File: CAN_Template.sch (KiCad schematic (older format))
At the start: 18 parts, among them U5 MCP2515-xSO, U6 SN65HVD1050D

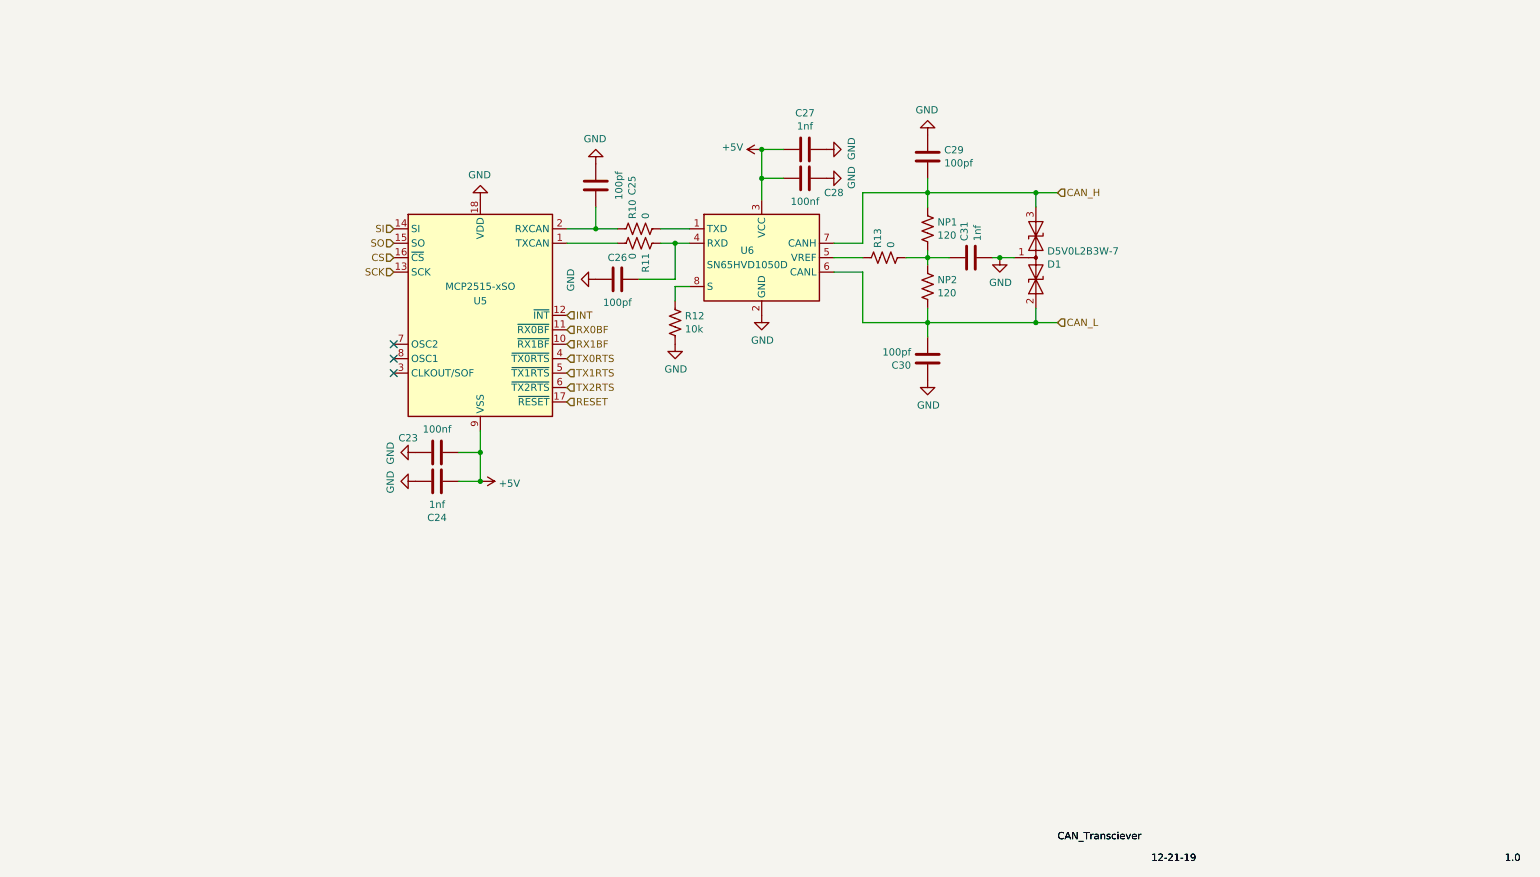
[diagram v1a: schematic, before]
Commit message: Changed filter and fixed CAN circuit
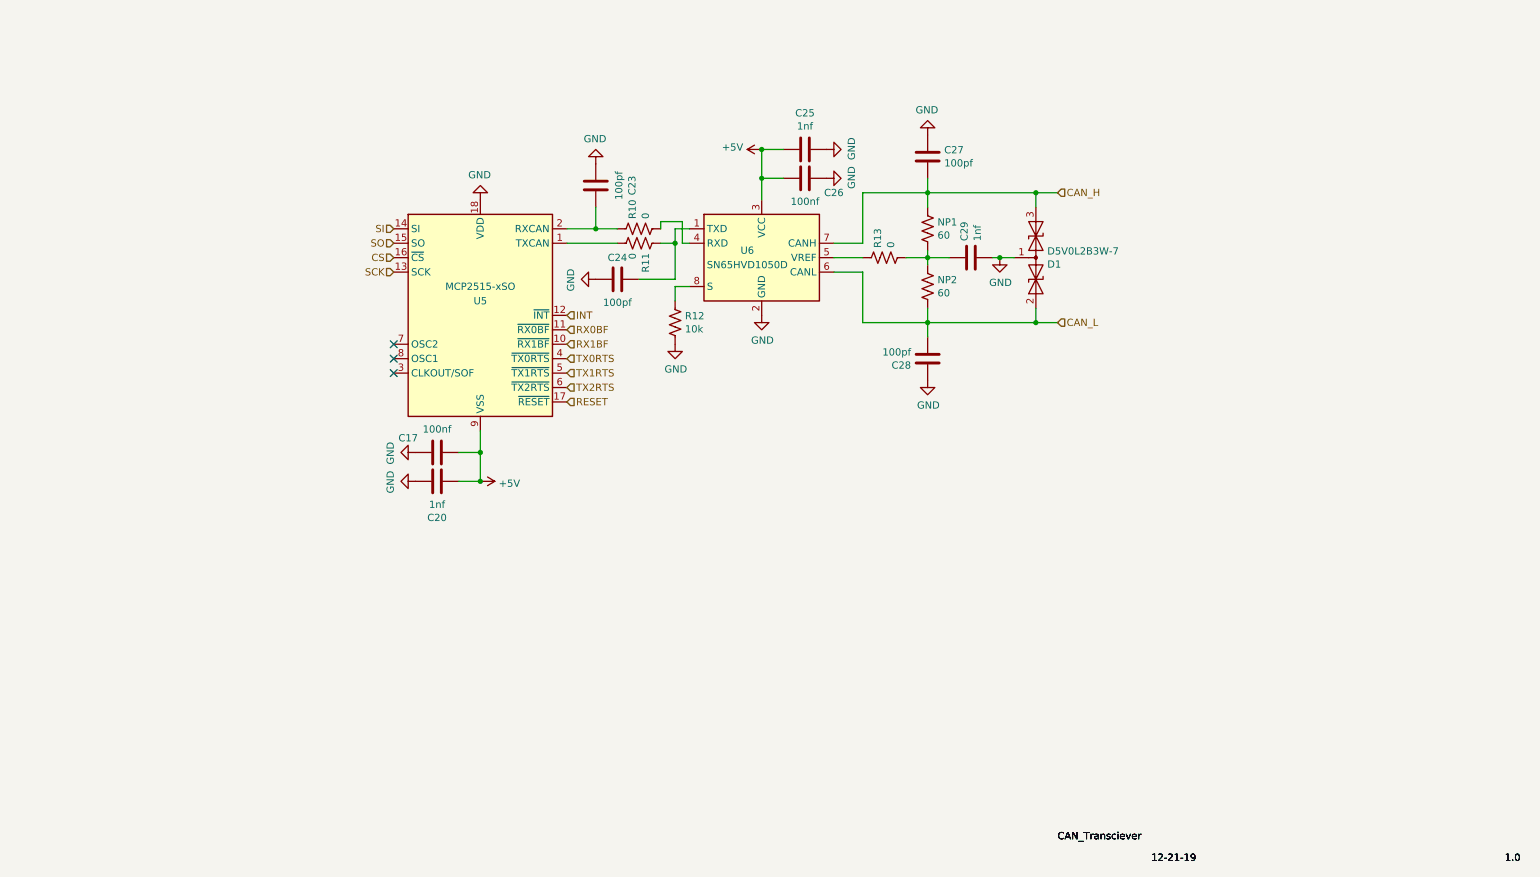
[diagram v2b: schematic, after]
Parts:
- NP1, NP2: value 120 -> 60
- renumbered C23 to C17, C24 to C20, C25 to C23, C26 to C24, C27 to C25, C28 to C26, C29 to C27, C30 to C28, C31 to C29
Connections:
- net at U6.1 (TXD): now also C24.2, R11.1; no longer R10.2
- new net: R10.2, U6.4 (RXD)
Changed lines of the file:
@@
 EESchema Schematic File Version 4
 LIBS:BLEANT-cache
+LIBS:CAN_Template-cache
 EELAYER 30 0
 EELAYER END
@@
 Text Label 7500 7500 0    50   ~ 0
 CAN_Transciever
+Text Label 10600 7650 0    50   ~ 0
+1.0
+Text Label 8150 7650 0    50   ~ 0
+12-21-19
+Text Label 7500 7500 0    50   ~ 0
+CAN_Transciever
 $Comp
 L Device:R_US NP1
@@
 P 6600 3250
 F 0 "NP1" H 6668 3296 50  0000 L CNN
-F 1 "120" H 6668 3205 50  0000 L CNN
+F 1 "60" H 6668 3205 50  0000 L CNN
 F 2 "Resistor_SMD:R_0402_1005Metric" V 6640 3240 50  0001 C CNN
 F 3 "~" H 6600 3250 50  0001 C CNN
@@
 $EndComp
 $Comp
-L Device:C C25
+L Device:C C23
 U 1 1 5DCB7D7B
 P 4300 2950
-F 0 "C25" V 4048 2950 50  0000 C CNN
+F 0 "C23" V 4048 2950 50  0000 C CNN
 F 1 "100pf" V 4139 2950 50  0000 C CNN
 F 2 "Capacitor_SMD:C_0402_1005Metric" H 4338 2800 50  0001 C CNN
@@
 $EndComp
 $Comp
-L Device:C C27
+L Device:C C25
 U 1 1 5DCB9CD1
 P 5750 2700
-F 0 "C27" V 5498 2700 50  0000 C CNN
+F 0 "C25" V 5498 2700 50  0000 C CNN
 F 1 "1nf" V 5589 2700 50  0000 C CNN
 F 2 "Capacitor_SMD:C_0402_1005Metric" H 5788 2550 50  0001 C CNN
@@
 $EndComp
 $Comp
-L Device:C C28
+L Device:C C26
 U 1 1 5DCBAD85
 P 5750 2900
-F 0 "C28" V 5650 2700 50  0000 C CNN
+F 0 "C26" V 5650 2700 50  0000 C CNN
 F 1 "100nf" V 5589 2900 50  0000 C CNN
 F 2 "Capacitor_SMD:C_0402_1005Metric" H 5788 2750 50  0001 C CNN
@@
 $EndComp
 $Comp
-L Device:C C30
+L Device:C C28
 U 1 1 5DCE6703
 P 6600 4150
-F 0 "C30" H 6715 4196 50  0000 L CNN
+F 0 "C28" H 6715 4196 50  0000 L CNN
 F 1 "100pf" H 6715 4105 50  0000 L CNN
 F 2 "Capacitor_SMD:C_0402_1005Metric" H 6638 4000 50  0001 C CNN
@@
 P 6600 3650
 F 0 "NP2" H 6668 3696 50  0000 L CNN
-F 1 "120" H 6668 3605 50  0000 L CNN
+F 1 "60" H 6668 3605 50  0000 L CNN
 F 2 "Resistor_SMD:R_0402_1005Metric" V 6640 3640 50  0001 C CNN
 F 3 "~" H 6600 3650 50  0001 C CNN
@@
 $EndComp
 $Comp
-L Device:C C31
+L Device:C C29
 U 1 1 5DCEFDFD
 P 6900 3450
-F 0 "C31" H 7015 3496 50  0000 L CNN
+F 0 "C29" H 7015 3496 50  0000 L CNN
 F 1 "1nf" H 7015 3405 50  0000 L CNN
 F 2 "Capacitor_SMD:C_0402_1005Metric" H 6938 3300 50  0001 C CNN
@@
 $EndComp
 $Comp
+L Device:D_TVS_x2_CAA D1
+U 1 1 5DD0169A
+P 7350 3450
+F 0 "D1" V 7304 3529 50  0000 L CNN
+F 1 "D5V0L2B3W-7" V 7395 3529 50  0000 L CNN
+F 2 "Package_TO_SOT_SMD:SOT-23" H 7200 3450 50  0001 C CNN
+F 3 "https://www.mouser.com/datasheet/2/115/D5V0L2B3W-218988.pdf" H 7200 3450 50  0001 C CNN
+	1    7350 3450
+	0    1    -1   0
+$EndComp
+$Comp
 L Device:R_US R12
 U 1 1 5DD5BD7B
@@
 CAN_H
 $Comp
-L Device:C C29
+L Device:C C27
 U 1 1 5DCE5998
 P 6600 2750
-F 0 "C29" H 6715 2796 50  0000 L CNN
+F 0 "C27" H 6715 2796 50  0000 L CNN
 F 1 "100pf" H 6715 2705 50  0000 L CNN
 F 2 "Capacitor_SMD:C_0402_1005Metric" H 6638 2600 50  0001 C CNN
@@
 $EndComp
 $Comp
-L Device:C C24
+L Device:C C20
 U 1 1 5E0BDAE5
 P 3200 5000
-F 0 "C24" V 2948 5000 50  0000 C CNN
+F 0 "C20" V 2948 5000 50  0000 C CNN
 F 1 "1nf" V 3039 5000 50  0000 C CNN
 F 2 "Capacitor_SMD:C_0402_1005Metric" H 3238 4850 50  0001 C CNN
@@
 $EndComp
 $Comp
-L Device:C C23
+L Device:C C17
 U 1 1 5E0BDAEB
 P 3200 4800
-F 0 "C23" V 3100 4600 50  0000 C CNN
+F 0 "C17" V 3100 4600 50  0000 C CNN
 F 1 "100nf" V 3039 4800 50  0000 C CNN
 F 2 "Capacitor_SMD:C_0402_1005Metric" H 3238 4650 50  0001 C CNN
@@
 Connection ~ 3500 5000
 $Comp
-L Device:C C26
+L Device:C C24
 U 1 1 5E0C191D
 P 4450 3600
-F 0 "C26" V 4600 3600 50  0000 C CNN
+F 0 "C24" V 4600 3600 50  0000 C CNN
 F 1 "100pf" V 4289 3600 50  0000 C CNN
 F 2 "Capacitor_SMD:C_0402_1005Metric" H 4488 3450 50  0001 C CNN
@@
 Wire Wire Line
 	4850 3600 4850 3350
-Connection ~ 4850 3350
-Wire Wire Line
-	4850 3350 4950 3350
 Wire Wire Line
 	4300 3100 4300 3250
@@
 Wire Wire Line
 	4300 3250 4450 3250
-Wire Wire Line
-	4750 3250 4950 3250
 NoConn ~ 2900 4050
 NoConn ~ 2900 4150
@@
 Text Label 7500 7500 0    50   ~ 0
 CAN_Transciever
-$Comp
-L Device:D_TVS_x2_CAA D1
-U 1 1 5DD0169A
-P 7350 3450
-F 0 "D1" V 7304 3529 50  0000 L CNN
-F 1 "D5V0L2B3W-7" V 7395 3529 50  0000 L CNN
-F 2 "Package_TO_SOT_SMD:SOT-23" H 7200 3450 50  0001 C CNN
-F 3 "https://www.mouser.com/datasheet/2/115/D5V0L2B3W-218988.pdf" H 7200 3450 50  0001 C CNN
-	1    7350 3450
-	0    1    -1   0
-$EndComp
+Wire Wire Line
+	4850 3350 4850 3250
+Wire Wire Line
+	4850 3250 4950 3250
+Connection ~ 4850 3350
+Wire Wire Line
+	4750 3250 4750 3200
+Wire Wire Line
+	4750 3200 4900 3200
+Wire Wire Line
+	4900 3200 4900 3350
+Wire Wire Line
+	4900 3350 4950 3350
 $EndSCHEMATC

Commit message: Added a level shifter
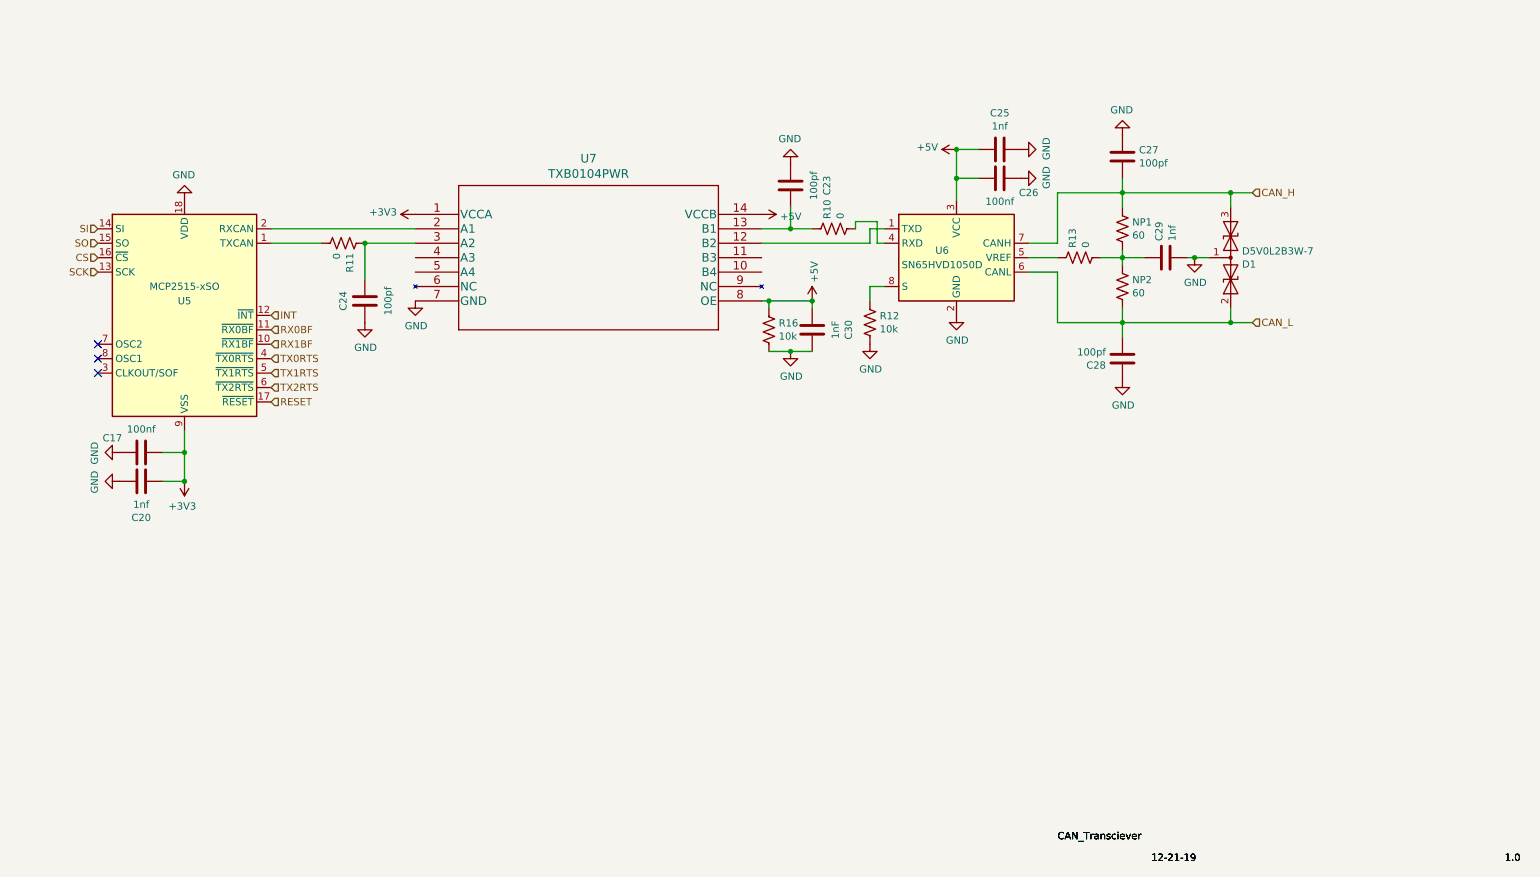
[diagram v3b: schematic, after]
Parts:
- added C30: 1nF, Capacitor_SMD:C_0402_1005Metric, symbol Device:C
- added R16: 10k, Resistor_SMD:R_0402_1005Metric, symbol Device:R_US
- added U7: TXB0104PWR, Level Shifter:TXB0104PWR, symbol 2019-12-30_17-25-07:TXB0104PWR
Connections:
- net +5V: now also C30.2, R16.1, U7.14 (VCCB), U7.8 (OE); no longer C17.1, C20.2, U5.9 (VSS)
- net GND: now also C30.1, R16.2, U7.7 (GND)
- net at C23.1, R10.1: now also U7.13 (B1); no longer U5.2 (RXCAN)
- net at C24.2, R11.1: now also U7.3 (A2); no longer U6.1 (TXD)
- new net: U5.2 (RXCAN), U7.2 (A1)
- new net: U6.1 (TXD), U7.12 (B2)
- new net +3V3: C17.1, C20.2, U5.9 (VSS), U7.1 (VCCA)
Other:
- moved on the sheet: C17, C20, C23, C24, C25, C26, C27, C28, C29, D1, NP1, NP2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

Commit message: Added a metric ton of test points
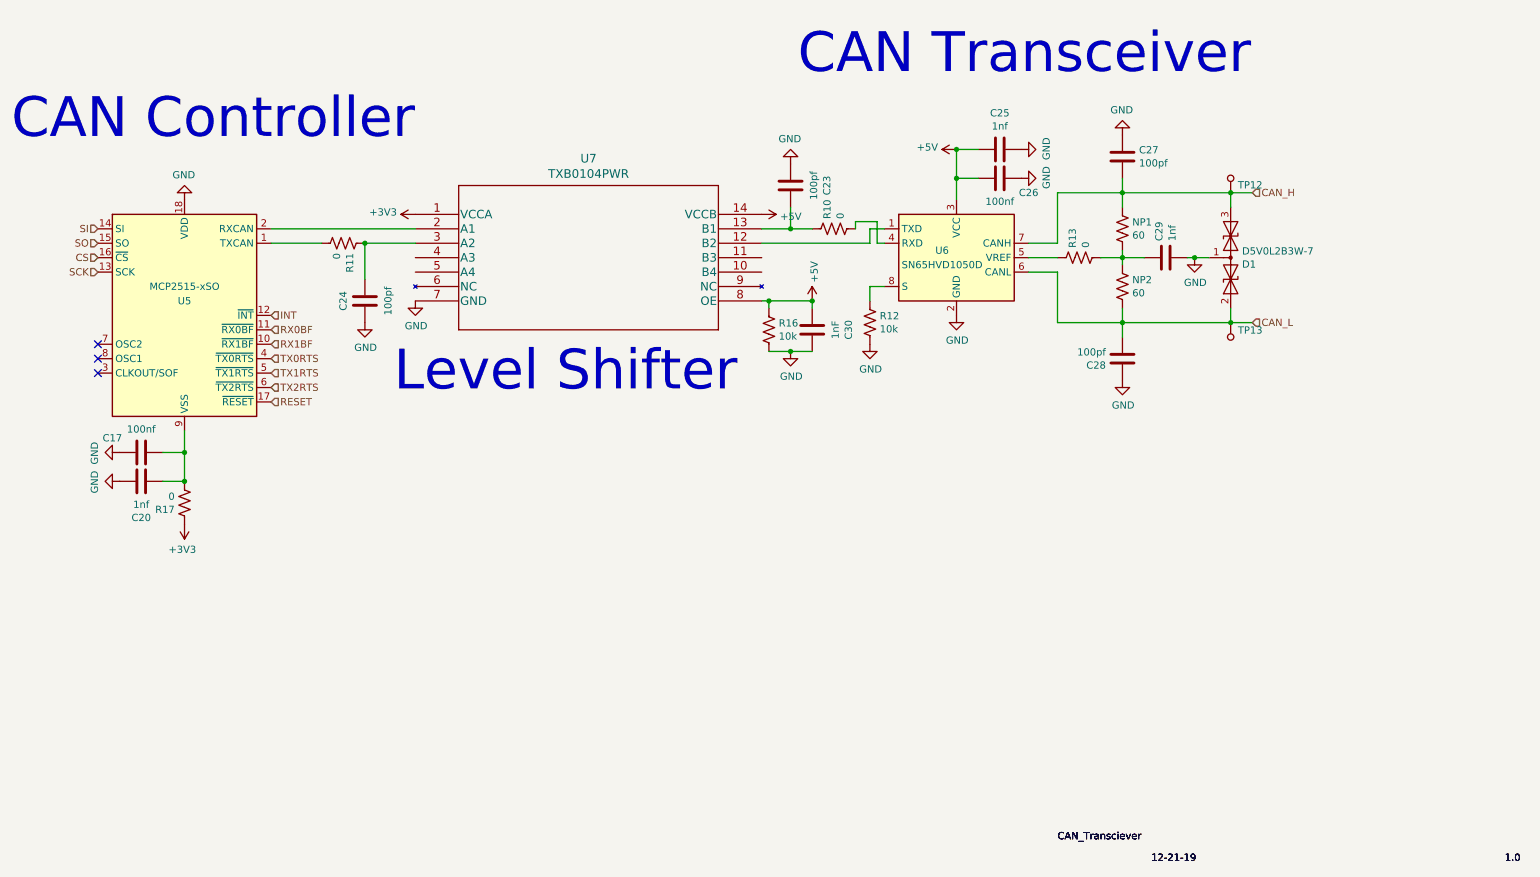
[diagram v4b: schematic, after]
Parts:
- added R17: 0, Resistor_SMD:R_0402_1005Metric, symbol Device:R_US
- added TP12, TP13: 5029, digikey-footprints:PC_Test_Point_Mini_3.8x2.03mm, symbol dk_Test-Points:5029
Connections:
- net +3V3: now also R17.1; no longer C17.1, C20.2, U5.9 (VSS)
- net CAN_H: now also TP12.1
- net CAN_L: now also TP13.1
- new net: C17.1, C20.2, R17.2, U5.9 (VSS)
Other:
- note added: "CAN Controller"
- note added: "CAN Transceiver\n"
- note added: "Level Shifter"
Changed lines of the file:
@@
 L power:+3V3 #PWR010
 U 1 1 5E0C8133
-P 1450 5000
-F 0 "#PWR010" H 1450 4850 50  0001 C CNN
-F 1 "+3V3" H 1465 5173 50  0000 C CNN
-F 2 "" H 1450 5000 50  0001 C CNN
-F 3 "" H 1450 5000 50  0001 C CNN
-	1    1450 5000
+P 1450 5300
+F 0 "#PWR010" H 1450 5150 50  0001 C CNN
+F 1 "+3V3" H 1465 5473 50  0000 C CNN
+F 2 "" H 1450 5300 50  0001 C CNN
+F 3 "" H 1450 5300 50  0001 C CNN
+	1    1450 5300
 	-1   0    0    1
 $EndComp
@@
 Wire Wire Line
 	5650 4100 5800 4100
+Text Notes 2900 4400 0    276  ~ 0
+Level Shifter
+Text Notes 5700 2200 0    276  ~ 0
+CAN Transceiver\n
+Text Notes 250  2650 0    276  ~ 0
+CAN Controller
+$Comp
+L Device:R_US R17
+U 1 1 5E27A6F5
+P 1450 5150
+F 0 "R17" H 1518 5196 50  0000 L CNN
+F 1 "0" H 1518 5105 50  0000 L CNN
+F 2 "Resistor_SMD:R_0402_1005Metric" V 1490 5140 50  0001 C CNN
+F 3 "~" H 1450 5150 50  0001 C CNN
+	1    1450 5150
+	-1   0    0    1
+$EndComp
+$Comp
+L dk_Test-Points:5029 TP12
+U 1 1 5E2BCF1F
+P 8700 2900
+F 0 "TP12" H 8650 2947 50  0000 R CNN
+F 1 "5029" H 8700 2800 50  0001 C CNN
+F 2 "digikey-footprints:PC_Test_Point_Mini_3.8x2.03mm" H 8900 3100 60  0001 L CNN
+F 3 "http://www.keyelco.com/product-pdf.cfm?p=1358" H 8900 3200 60  0001 L CNN
+F 4 "36-5029CT-ND" H 8900 3300 60  0001 L CNN "Digi-Key_PN"
+F 5 "5029" H 8900 3400 60  0001 L CNN "MPN"
+F 6 "Test and Measurement" H 8900 3500 60  0001 L CNN "Category"
+F 7 "Test Points" H 8900 3600 60  0001 L CNN "Family"
+F 8 "http://www.keyelco.com/product-pdf.cfm?p=1358" H 8900 3700 60  0001 L CNN "DK_Datasheet_Link"
+F 9 "/product-detail/en/keystone-electronics/5029/36-5029CT-ND/5980631" H 8900 3800 60  0001 L CNN "DK_Detail_Page"
+F 10 "PC TEST POINT MINIATURE" H 8900 3900 60  0001 L CNN "Description"
+F 11 "Keystone Electronics" H 8900 4000 60  0001 L CNN "Manufacturer"
+F 12 "Active" H 8900 4100 60  0001 L CNN "Status"
+	1    8700 2900
+	-1   0    0    1
+$EndComp
+$Comp
+L dk_Test-Points:5029 TP13
+U 1 1 5E2BE1B4
+P 8700 4000
+F 0 "TP13" H 8750 4047 50  0000 L CNN
+F 1 "5029" H 8700 3900 50  0001 C CNN
+F 2 "digikey-footprints:PC_Test_Point_Mini_3.8x2.03mm" H 8900 4200 60  0001 L CNN
+F 3 "http://www.keyelco.com/product-pdf.cfm?p=1358" H 8900 4300 60  0001 L CNN
+F 4 "36-5029CT-ND" H 8900 4400 60  0001 L CNN "Digi-Key_PN"
+F 5 "5029" H 8900 4500 60  0001 L CNN "MPN"
+F 6 "Test and Measurement" H 8900 4600 60  0001 L CNN "Category"
+F 7 "Test Points" H 8900 4700 60  0001 L CNN "Family"
+F 8 "http://www.keyelco.com/product-pdf.cfm?p=1358" H 8900 4800 60  0001 L CNN "DK_Datasheet_Link"
+F 9 "/product-detail/en/keystone-electronics/5029/36-5029CT-ND/5980631" H 8900 4900 60  0001 L CNN "DK_Detail_Page"
+F 10 "PC TEST POINT MINIATURE" H 8900 5000 60  0001 L CNN "Description"
+F 11 "Keystone Electronics" H 8900 5100 60  0001 L CNN "Manufacturer"
+F 12 "Active" H 8900 5200 60  0001 L CNN "Status"
+	1    8700 4000
+	1    0    0    -1
+$EndComp
 $EndSCHEMATC

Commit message: Added some filters and stuff
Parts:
- removed R16: 10k, Resistor_SMD:R_0402_1005Metric, symbol Device:R_US
- removed U7: TXB0104PWR, Level Shifter:TXB0104PWR, symbol 2019-12-30_17-25-07:TXB0104PWR
- added C37, C38, C39: 10nF, Capacitor_SMD:C_0402_1005Metric, symbol Device:C
- added U2, U7: SN74LVC1T45DBVR, digikey-footprints:SOT-23-6, symbol dk_Logic-Translators-Level-Shifters:SN74LVC1T45DBVR
- C30: value 1nF -> 10nF
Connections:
- net +3V3: now also C30.2, C37.2, U2.1 (VCCA), U7.1 (VCCA), U7.5 (DIR)
- net +5V: now also C38.1, C39.1, U2.6 (VCCB), U7.6 (VCCB); no longer C30.2
- net GND: now also C37.1, C38.2, C39.2, U2.2 (GND), U2.5 (DIR), U7.2 (GND)
- net at U5.2 (RXCAN): now also U2.3 (A)
- net at C23.1, R10.1: now also U2.4 (B)
- net at U6.1 (TXD): now also U7.4 (B)
- net at C24.2, R11.1: now also U7.3 (A)
